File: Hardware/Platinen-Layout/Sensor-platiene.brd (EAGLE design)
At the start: 40.2 x 40.1 mm, 43 parts, among them J10 Flash Programming, J5 Flash Programming, U1 AS72651, U10 4MB Flash, U2 4MB Flash, U5 AS72653, U6 AS72652

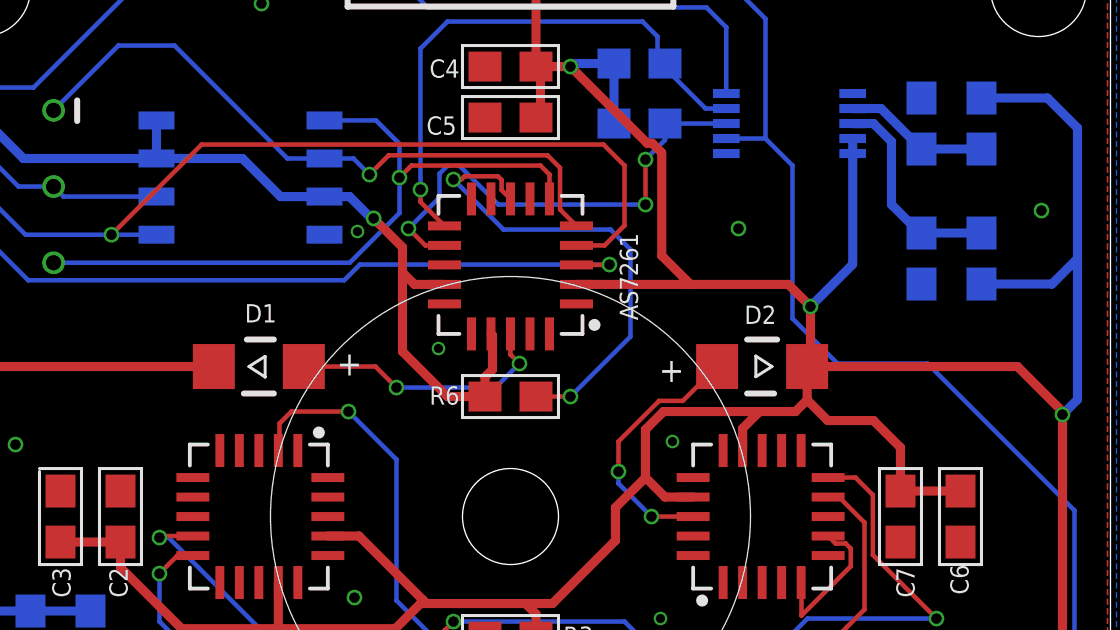
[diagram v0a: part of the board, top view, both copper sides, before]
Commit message: add write to db
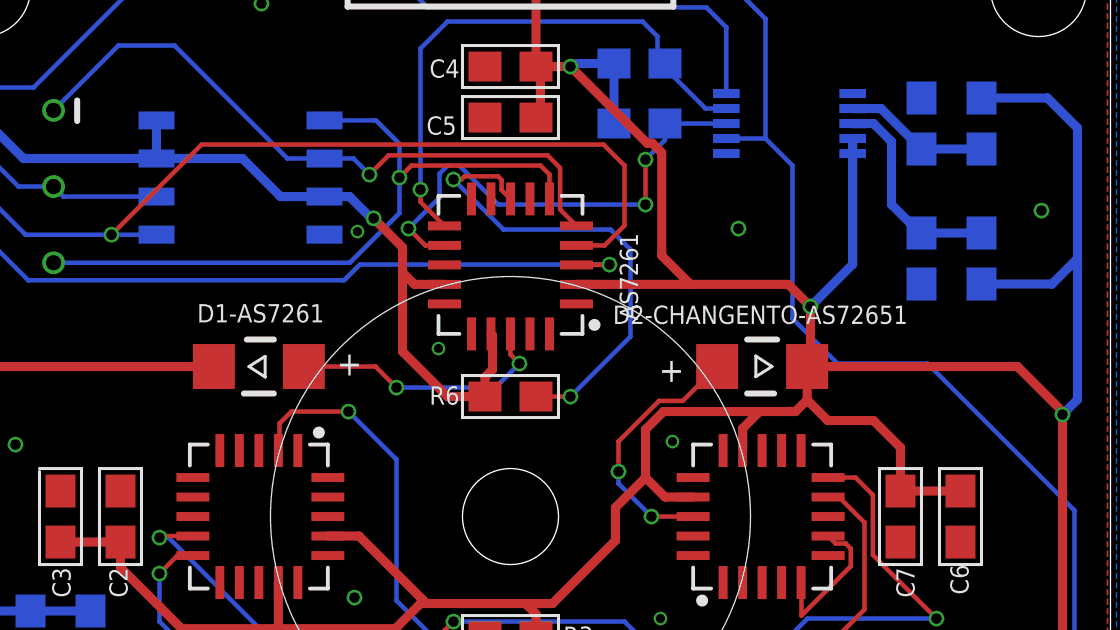
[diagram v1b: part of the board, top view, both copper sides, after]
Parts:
- renumbered D1 to D1-AS7261, D2 to D2-CHANGENTO-AS72651
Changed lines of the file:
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@@
 <?xml version="1.0" encoding="utf-8"?>
 <!DOCTYPE eagle SYSTEM "eagle.dtd">
-<eagle version="9.6.1">
+<eagle version="9.6.2">
 <drawing>
 <settings>
-<setting alwaysvectorfont="yes"/>
+<setting alwaysvectorfont="no"/>
 <setting verticaltext="up"/>
 </settings>
 <grid distance="0.01" unitdist="mm" unit="mm" style="dots" multiple="1" display="yes" altdistance="0.1" altunitdist="mm" altunit="mm"/>
 <layers>
-<layer number="1" name="Top" color="4" fill="1" visible="no" active="yes"/>
-<layer number="16" name="Bottom" color="1" fill="1" visible="no" active="yes"/>
+<layer number="1" name="Top" color="4" fill="1" visible="yes" active="yes"/>
+<layer number="16" name="Bottom" color="1" fill="1" visible="yes" active="yes"/>
 <layer number="17" name="Pads" color="2" fill="1" visible="yes" active="yes"/>
 <layer number="18" name="Vias" color="2" fill="1" visible="yes" active="yes"/>
@@
 <layer number="25" name="tNames" color="7" fill="1" visible="yes" active="yes"/>
 <layer number="26" name="bNames" color="7" fill="1" visible="yes" active="yes"/>
-<layer number="27" name="tValues" color="7" fill="1" visible="no" active="yes"/>
+<layer number="27" name="tValues" color="7" fill="1" visible="yes" active="yes"/>
 <layer number="28" name="bValues" color="7" fill="1" visible="no" active="yes"/>
 <layer number="29" name="tStop" color="7" fill="3" visible="no" active="yes"/>
@@
 <attribute name="VALUE" x="20" y="4.238" size="0.6096" layer="27" font="vector" ratio="20" align="top-center"/>
 </element>
-<element name="D1" library="150120RS75000_Eagle_WL-SMCW_rev20b" package="WL-SMCW_1206" package3d_urn="urn:adsk.eagle:package:19028166/2" value="" x="11.612" y="25" smashed="yes">
+<element name="D1-AS7261" library="150120RS75000_Eagle_WL-SMCW_rev20b" package="WL-SMCW_1206" package3d_urn="urn:adsk.eagle:package:19028166/2" value="" x="11.612" y="25" smashed="yes">
 <attribute name="ABSTRAHLWINKEL" value="140°" x="45.902" y="0.87" size="1.778" layer="27" display="off"/>
 <attribute name="CHIP-TECHNOLOGY" value="AlInGaP" x="45.902" y="0.87" size="1.778" layer="27" display="off"/>
@@
 <attribute name="VALUE" x="11.372" y="23.06" size="0.6096" layer="27" align="bottom-center"/>
 </element>
-<element name="D2" library="150120RS75000_Eagle_WL-SMCW_rev20b" package="WL-SMCW_1206" package3d_urn="urn:adsk.eagle:package:19028166/2" value="" x="28.388" y="25" smashed="yes" rot="R180">
+<element name="D2-CHANGENTO-AS72651" library="150120RS75000_Eagle_WL-SMCW_rev20b" package="WL-SMCW_1206" package3d_urn="urn:adsk.eagle:package:19028166/2" value="" x="28.388" y="25" smashed="yes" rot="R180">
 <attribute name="ABSTRAHLWINKEL" value="140°" x="-12.252" y="49.13" size="1.778" layer="27" rot="R180" display="off"/>
 <attribute name="CHIP-TECHNOLOGY" value="AlInGaP" x="-12.252" y="49.13" size="1.778" layer="27" rot="R180" display="off"/>
@@
 <contactref element="U10" pad="3"/>
 <contactref element="J10" pad="2"/>
-<contactref element="D2" pad="1"/>
-<contactref element="D1" pad="1"/>
+<contactref element="D2-CHANGENTO-AS72651" pad="1"/>
+<contactref element="D1-AS7261" pad="1"/>
 <contactref element="U$1" pad="4"/>
 <contactref element="U$1" pad="5"/>
@@
 <signal name="N$1">
 <contactref element="AS7261" pad="18"/>
-<contactref element="D1" pad="2"/>
+<contactref element="D1-AS7261" pad="2"/>
 <wire x1="20" y1="26.088" x2="20" y2="25.4" width="0.1524" layer="1"/>
 <wire x1="20" y1="25.4" x2="20.3" y2="25.1" width="0.1524" layer="1"/>
@@
 <signal name="N$4">
 <contactref element="U5" pad="18"/>
-<contactref element="D2" pad="2"/>
+<contactref element="D2-CHANGENTO-AS72651" pad="2"/>
 <via x="23.6" y="21.5" extent="1-16" drill="0.35"/>
 <wire x1="26.888" y1="25" x2="25.7436" y2="23.8556" width="0.1524" layer="1"/>
